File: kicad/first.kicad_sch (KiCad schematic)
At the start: 103 parts, among them J1 Conn_01x04_Pin, P1 USB_C_Plug_USB2.0, Q1 MMUN2111LT1G, Q2 MMBT3904, Q3 MMUN2111LT1G, Q4 MMBT3904, SW1 SW_SPDT, SW2 RotaryEncoder_Switch_MP, SW3 RotaryEncoder_Switch_MP, SW4 RotaryEncoder_Switch_MP, U1 OPA1678, U1 STM32F407VETx, U2 LP5907MFX-3.3, U2 OPA1678, U3 CS4272, U3 OPA1678, Y1 16 MHz

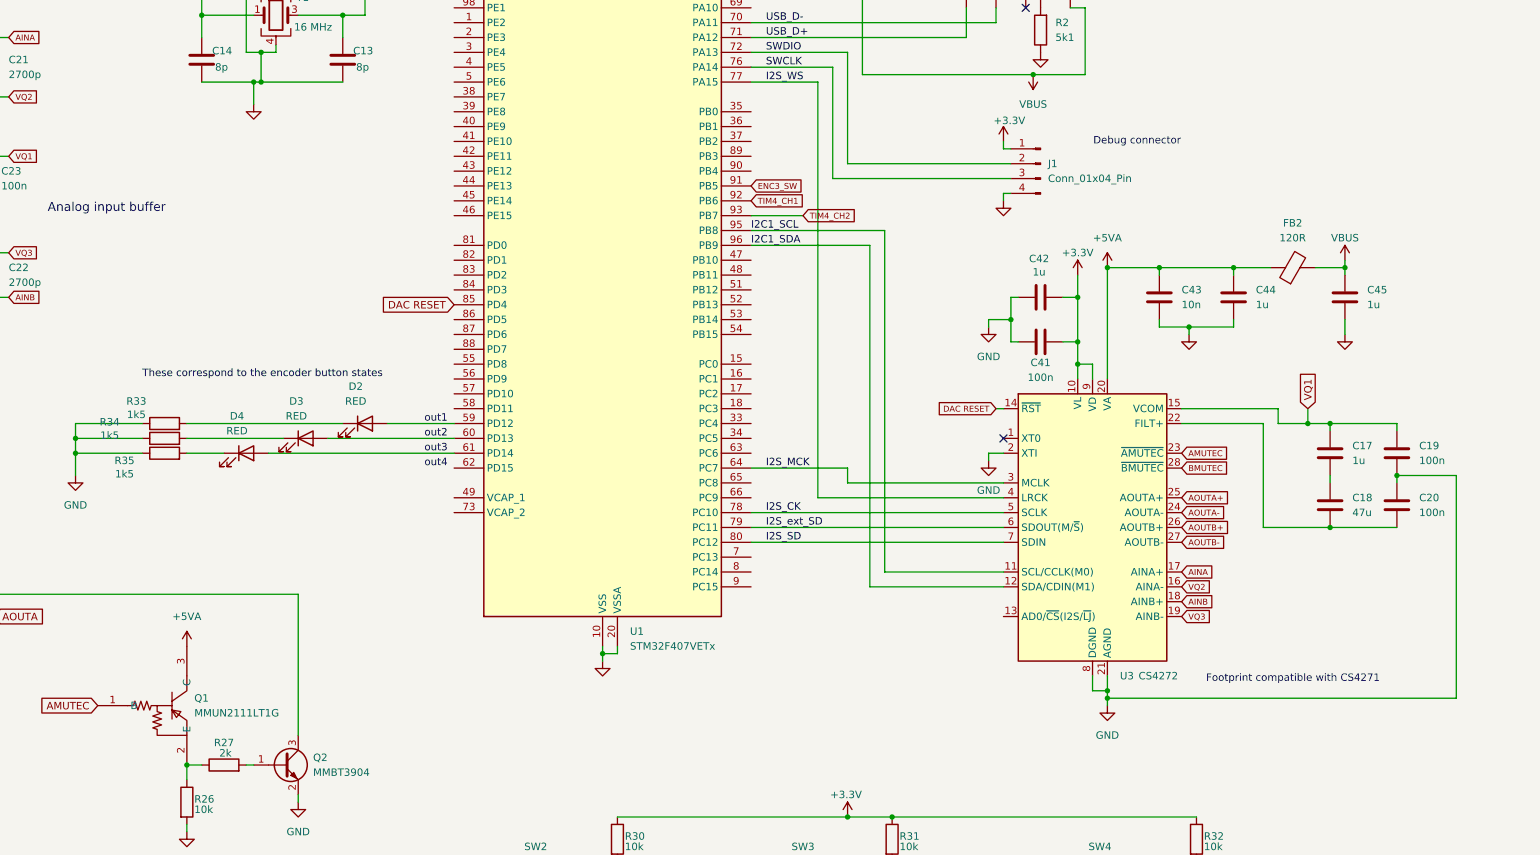
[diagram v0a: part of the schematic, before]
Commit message: assigned UART, I2C, SPI and some additional GPIOS
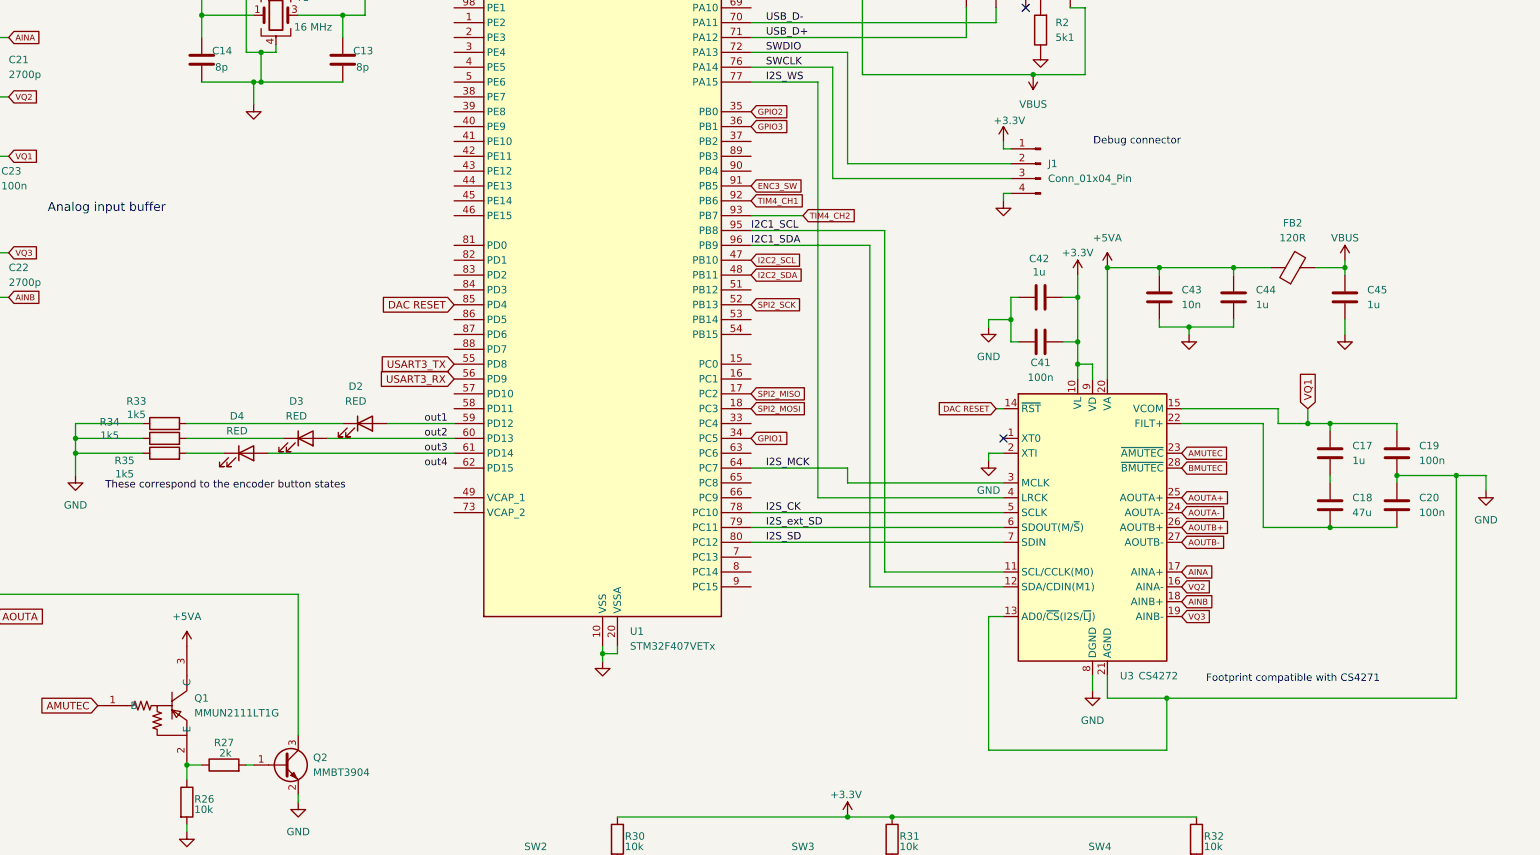
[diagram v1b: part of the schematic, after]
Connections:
- net GND: now also U3.13 (AD0/~{CS}(I2S/~{LJ}))
- net SPI2_MISO: now reaches U1.17 (PC2)
- net SPI2_MOSI: now reaches U1.18 (PC3)
- net GPIO1: now reaches U1.34 (PC5)
- net GPIO2: now reaches U1.35 (PB0)
- net GPIO3: now reaches U1.36 (PB1)
- net I2C2_SCL: now reaches U1.47 (PB10)
- net I2C2_SDA: now reaches U1.48 (PB11)
- net SPI2_SCK: now reaches U1.52 (PB13)
- net USART3_TX: now reaches U1.55 (PD8)
- net USART3_RX: now reaches U1.56 (PD9)

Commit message: a
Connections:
- net +3.3VA: now also U1.21 (VREF+)
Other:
- note added: "AN4488"
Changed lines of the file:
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@@
 		)
 	)
+	(text "AN4488"
+		(exclude_from_sim no)
+		(at 169.418 29.464 0)
+		(effects
+			(font
+				(size 1.778 1.778)
+			)
+		)
+	)
 	(text "Analog output filters"
 		(exclude_from_sim no)
@@
 		(effects
 			(font
-				(size 0.508 0.508)
+				(size 0.635 0.635)
 			)
 			(justify left bottom)
@@
 					(unit 1)
 				)
+			)
+		)
+	)
+	(symbol
+		(lib_id "power:+3.3VA")
+		(at 201.93 57.15 0)
+		(unit 1)
+		(body_style 1)
+		(exclude_from_sim no)
+		(in_bom yes)
+		(on_board yes)
+		(in_pos_files yes)
+		(dnp no)
+		(property "Reference" "#PWR047"
+			(at 201.93 60.96 0)
+			(hide yes)
+			(show_name no)
+			(do_not_autoplace no)
+			(effects
+				(font
+					(size 1.27 1.27)
+				)
+			)
+		)
+		(property "Value" "+3.3VA"
+			(at 197.866 56.642 0)
+			(show_name no)
+			(do_not_autoplace no)
+			(effects
+				(font
+					(size 1.27 1.27)
+				)
+			)
+		)
+		(property "Footprint" ""
+			(at 201.93 57.15 0)
+			(hide yes)
+			(show_name no)
+			(do_not_autoplace no)
+			(effects
+				(font
+					(size 1.27 1.27)
+				)
+			)
+		)
+		(property "Datasheet" ""
+			(at 201.93 57.15 0)
+			(hide yes)
+			(show_name no)
+			(do_not_autoplace no)
+			(effects
+				(font
+					(size 1.27 1.27)
+				)
+			)
+		)
+		(property "Description" "Power symbol creates a global label with name \"+3.3VA\""
+			(at 201.93 57.15 0)
+			(hide yes)
+			(show_name no)
+			(do_not_autoplace no)
+			(effects
+				(font
+					(size 1.27 1.27)
+				)
+			)
+		)
+		(pin "1"
+		)
+		(instances
+			(project "first"
+				(path "/580becc7-fa47-4b4d-a43e-4b9316967eb7"
+					(reference "#PWR047")
+					(unit 1)
+				)

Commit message: fixed error with codec reference decoupling, and value of VA decoupling
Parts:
- C9: value 10n -> 100n
- R3: value R -> 1k5
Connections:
- net GND: now also C17.2, C18.1
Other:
- note added: "Pick good LED for 2mA"
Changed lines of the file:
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@@
 	(generator_version "10.0")
 	(paper "A3")
+	(text "Pick good LED for 2mA"
+		(exclude_from_sim no)
+		(at 387.604 30.988 0)
+		(effects
+			(font
+				(size 1.27 1.27)
+			)
+		)
+	)
 	(text "Analog input buffer"
 		(exclude_from_sim no)
@@
 	)
 	(junction
+		(at 351.79 152.4)
+		(diameter 0)
+		(color 0 0 0 0)
+	)
+	(junction
 		(at 300.99 83.82)
 		(diameter 0)
@@
 	(wire
 		(pts
+			(xy 351.79 152.4) (xy 363.22 152.4)
+		)
+		(stroke
+			(width 0)
+			(type default)
+		)
+	)
+	(wire
+		(pts
 			(xy 269.24 210.82) (xy 276.86 210.82)
 		)
@@
 			)
 		)
-		(property "Value" "R"
+		(property "Value" "1k5"
 			(at 375.92 36.8299 0)
 			(show_name no)
@@
 			)
 		)
-		(property "Value" "10n"
+		(property "Value" "100n"
 			(at 254 34.2899 0)
 			(show_name no)

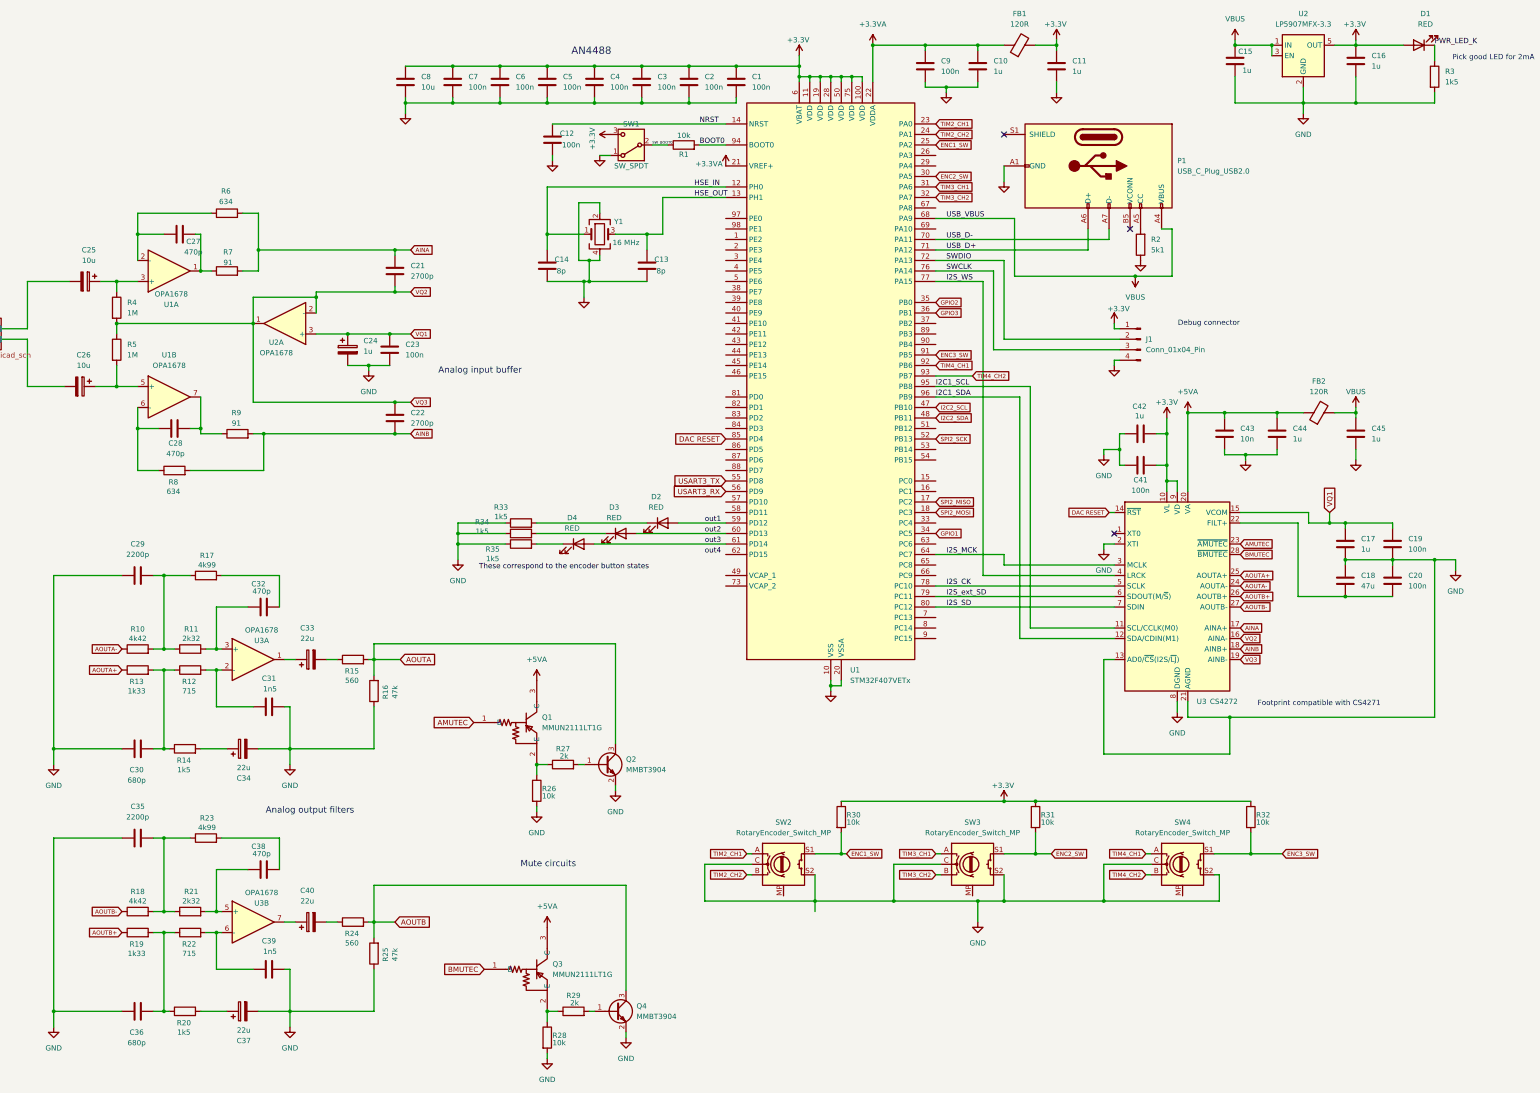
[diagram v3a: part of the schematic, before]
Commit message: decoupling cleanup, new LDO, I2C pullups
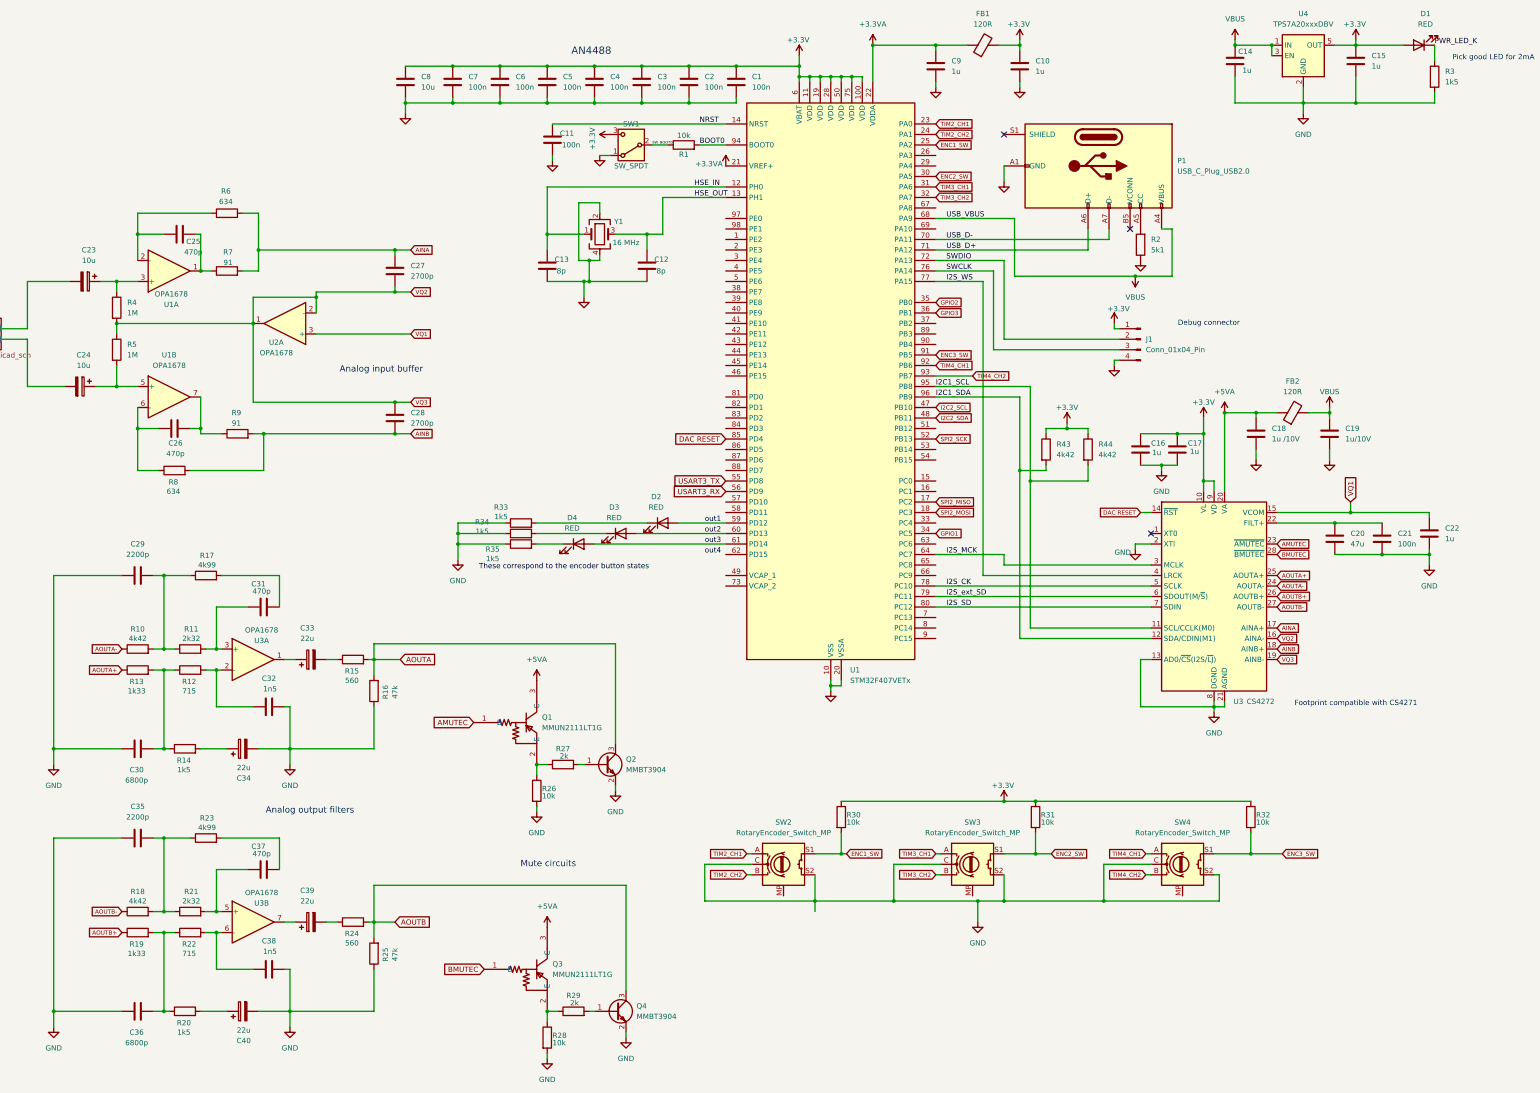
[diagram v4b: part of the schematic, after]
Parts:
- removed C19, C23, C41, C9: 100n, symbol Device:C
- removed C24: 1u, symbol Device:C_Polarized
- removed C42: 1u, symbol Device:C
- removed C43: 10n, symbol Device:C
- removed U2: LP5907MFX-3.3, Package_TO_SOT_SMD:SOT-23-5, symbol Regulator_Linear:LP5907MFX-3.3
- added C16, C17: 1u, symbol Device:C
- added R43, R44: 4k42, symbol Device:R
- added U4: TPS7A20xxxDBV, Package_TO_SOT_SMD:SOT-23-5, symbol Regulator_Linear:TPS7A20xxxDBV
- C18: renamed from C44; value 1u -> 1u /10V
- C19: renamed from C45; value 1u -> 1u/10V
- C30, C36: value 680p -> 6800p
- renumbered C11 to C10, C12 to C11, C13 to C12, C14 to C13, C15 to C14, C16 to C15, C18 to C20, C20 to C21, C17 to C22, C25 to C23, C26 to C24, C27 to C25, C28 to C26, C21 to C27, C22 to C28, C32 to C31, C31 to C32, C38 to C37, C39 to C38, C40 to C39, C37 to C40, C10 to C9
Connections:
- net +3.3V: now also C16.1, C17.1, R43.1, R44.1, U4.5 (OUT)
- net GND: now also C20.2, C21.2, C16.2, C17.2, U4.2 (GND); no longer C20.1, C21.1
- net I2C1_SCL: now also R44.2
- net I2C1_SDA: now also R43.2
- net VBUS: now also U4.1 (IN), U4.3 (EN)
- new net: C20.1, C21.1, U3.22 (FILT+)
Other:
- moved on the sheet: C10, C18, C19, C20, C21, C22, C9, FB1, FB2, U3
